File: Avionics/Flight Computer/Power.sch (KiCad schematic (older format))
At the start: 18 parts, among them U8 TPS54232

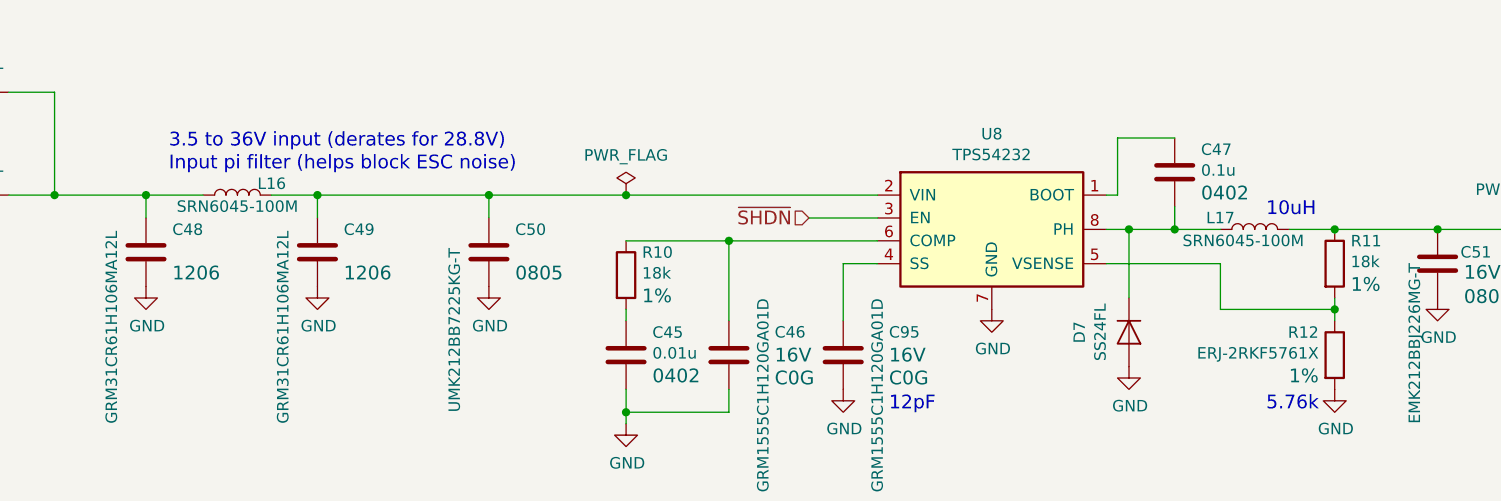
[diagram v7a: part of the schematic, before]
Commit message: Reduced inductor size at small efficiency cost.
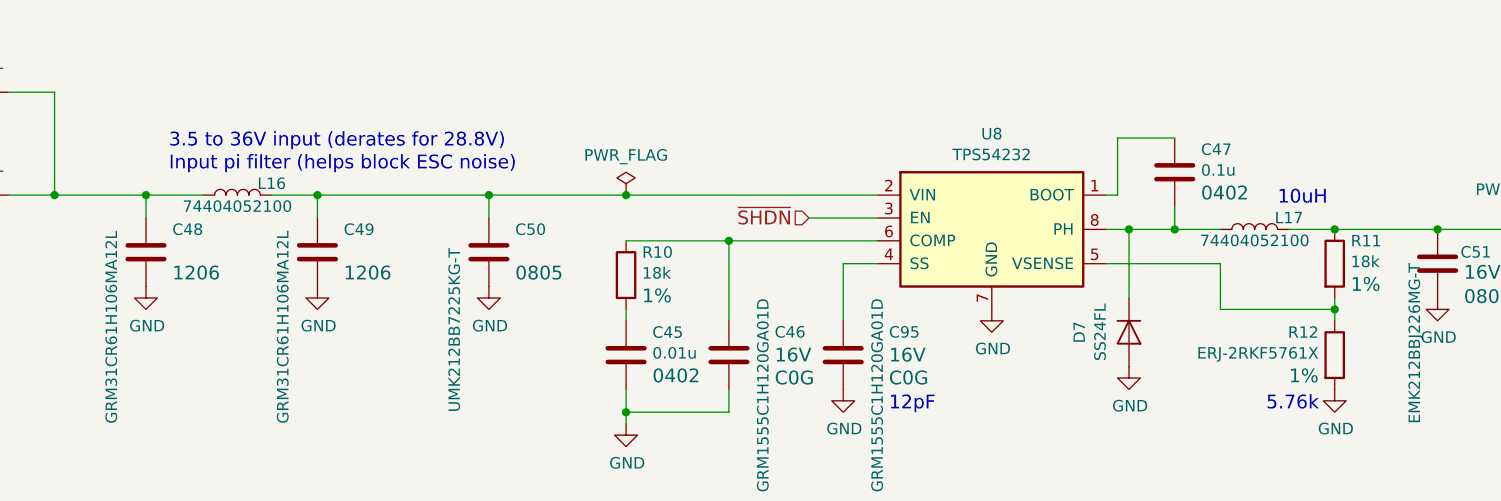
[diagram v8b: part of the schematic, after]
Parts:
- L16, L17: value SRN6045-100M -> 74404052100; footprint Inductors_SMD:L_BOURNS-SRN6045 -> Inductors:Inductor_Wurth_LQS-5020
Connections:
- net +3V3: now also L17.2; no longer L17.1
- net at C47.1, D7.1 (K), U8.8 (PH): now also L17.1; no longer L17.2
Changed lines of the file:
@@
 P 3550 3750
 F 0 "L16" V 3600 3600 50  0000 C CNN
-F 1 "SRN6045-100M" V 3500 3750 50  0000 C CNN
-F 2 "Inductors_SMD:L_BOURNS-SRN6045" H -1600 450 50  0001 C CNN
-F 3 "http://www.bourns.com/docs/Product-Datasheets/SRN6045.pdf" H -1600 450 50  0001 C CNN
+F 1 "74404052100" V 3500 3750 50  0000 C CNN
+F 2 "Inductors:Inductor_Wurth_LQS-5020" H -1600 450 50  0001 C CNN
+F 3 "http://katalog.we-online.de/pbs/datasheet/74404052100.pdf" H -1600 450 50  0001 C CNN
 	1    3550 3750
 	0    -1   -1   0
@@
 	1    0    0    -1
 $EndComp
-$Comp
-L L L17
-U 1 1 58E2BA02
-P 8000 3900
-F 0 "L17" V 8050 3750 50  0000 C CNN
-F 1 "SRN6045-100M" V 7950 3850 50  0000 C CNN
-F 2 "Inductors_SMD:L_BOURNS-SRN6045" H 2850 600 50  0001 C CNN
-F 3 "http://www.bourns.com/docs/Product-Datasheets/SRN6045.pdf" H 2850 600 50  0001 C CNN
-	1    8000 3900
-	0    1    -1   0
-$EndComp
 Wire Wire Line
 	6050 3850 6350 3850
@@
 Wire Wire Line
 	8150 3900 9650 3900
-Text Notes 8050 3850 0    60   ~ 0
+Text Notes 8100 3800 0    60   ~ 0
 10uH
 Connection ~ 8350 3900
@@
 $EndComp
 Connection ~ 5250 3750
+$Comp
+L L L17
+U 1 1 58E46EFA
+P 8000 3900
+F 0 "L17" V 8050 3750 50  0000 C CNN
+F 1 "74404052100" V 7950 3900 50  0000 C CNN
+F 2 "Inductors:Inductor_Wurth_LQS-5020" H 2850 600 50  0001 C CNN
+F 3 "http://katalog.we-online.de/pbs/datasheet/74404052100.pdf" H 2850 600 50  0001 C CNN
+	1    8000 3900
+	0    -1   -1   0
+$EndComp
 $EndSCHEMATC
